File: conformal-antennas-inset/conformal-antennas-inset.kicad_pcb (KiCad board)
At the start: 2 copper layers, 172.5 x 134.5 mm, 1 part, among them J1 Conn_Coaxial

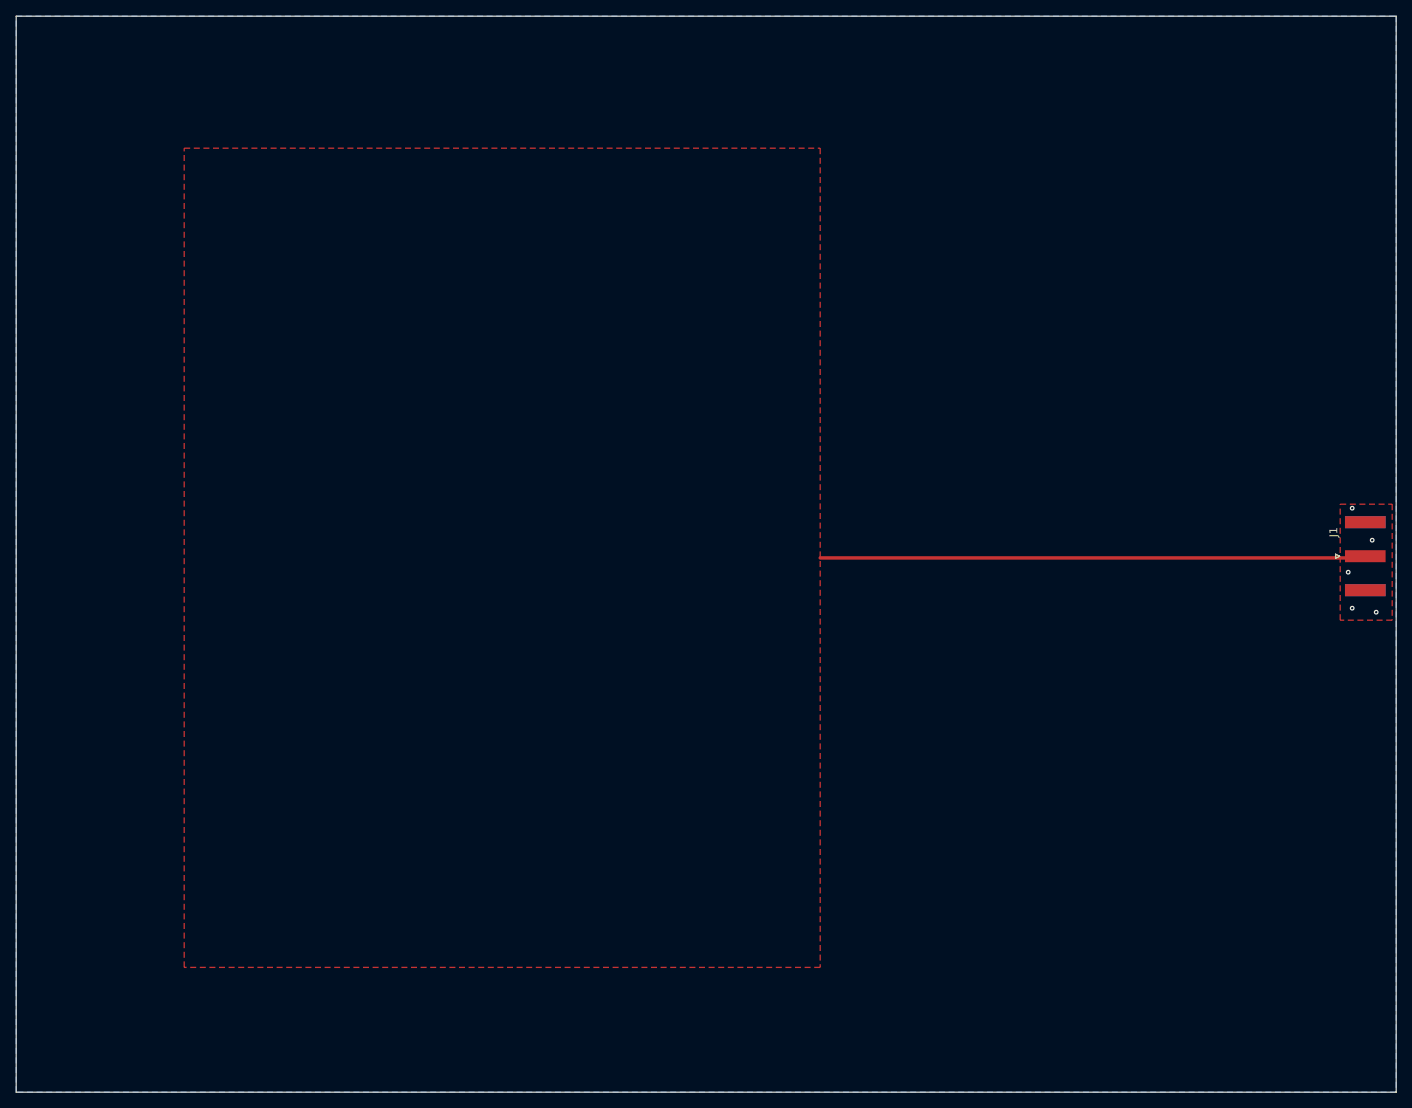
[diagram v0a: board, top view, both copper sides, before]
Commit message: resized ground plane
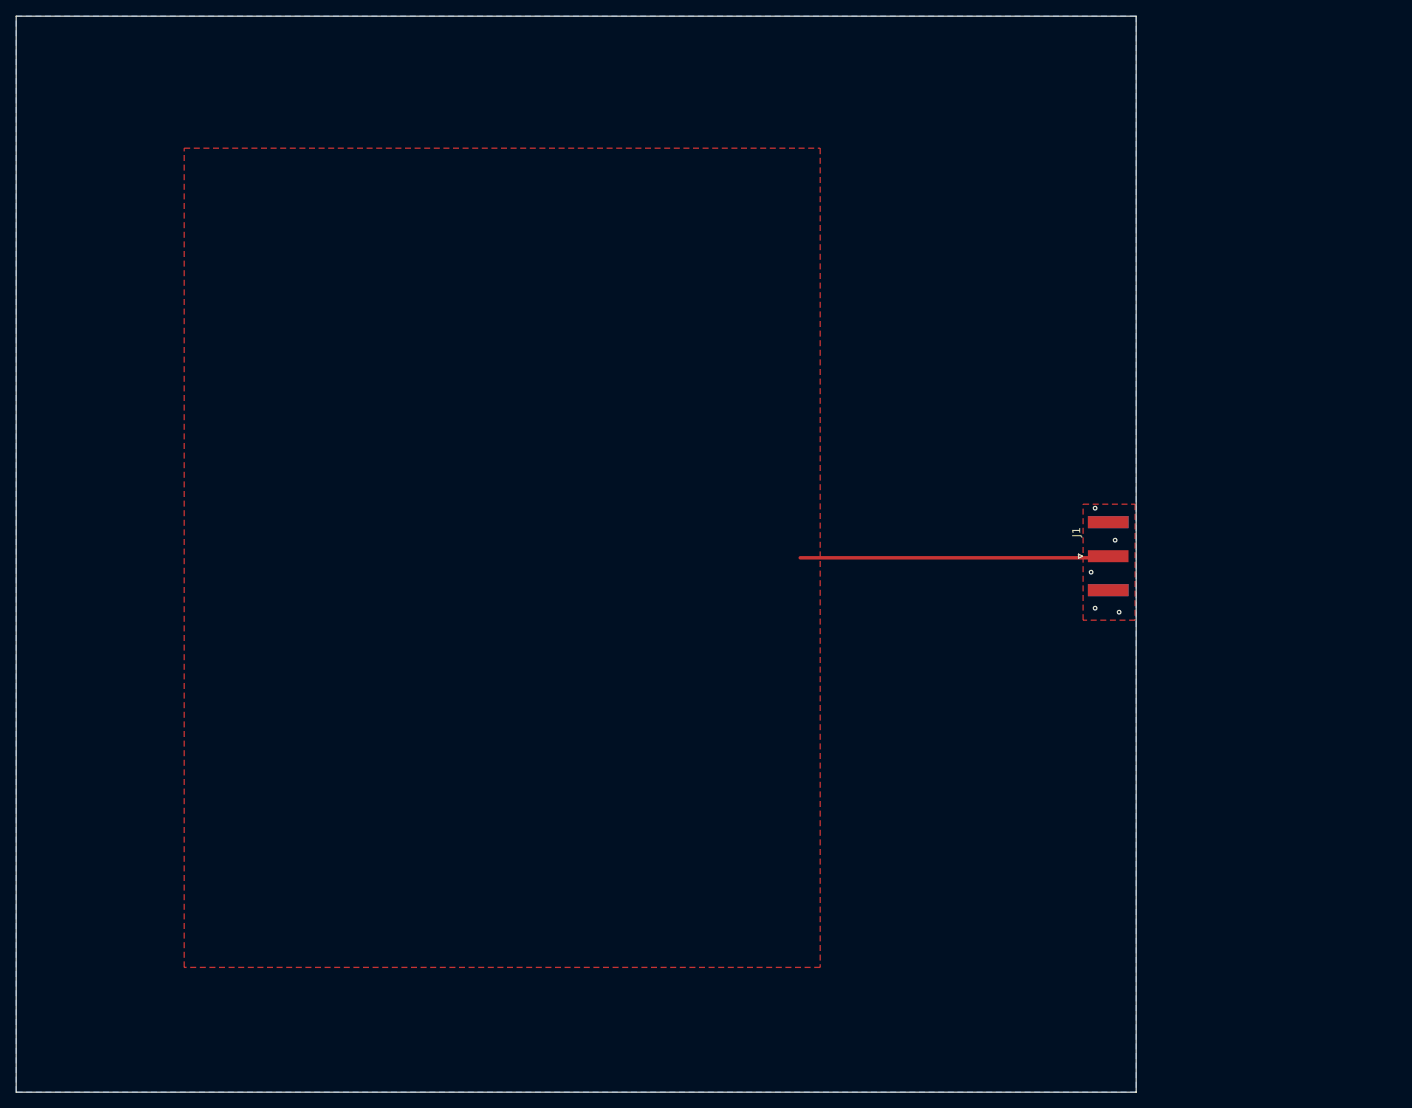
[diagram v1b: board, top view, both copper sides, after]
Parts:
- moved J1 32.1 mm to (185.0, 103.5)
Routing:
- net /Signal: track 68.1 -> 38.5 mm
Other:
- board size 172.5 x 134.5 mm -> 140 x 134.5 mm
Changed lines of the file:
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@@
 	(footprint "Connector_Coaxial:SMA_Amphenol_132289_EdgeMount"
 		(layer "F.Cu")
-		(at 217.1375 103.5)
+		(at 185 103.5)
 		(descr "https://www.amphenolrf.com/library/download/link/link_id/595984/parent/132289/")
 		(tags "SMA")
@@
 	(gr_line
 		(start 48.5 36)
-		(end 221 36)
+		(end 188.5 36)
 		(stroke
 			(width 0.05)
-			(type default)
+			(type solid)
 		)
 		(layer "Edge.Cuts")
 	)
 	(gr_line
-		(start 221 170.5)
+		(start 188.5 170.5)
 		(end 48.5 170.5)
 		(stroke
@@
 	)
 	(gr_line
-		(start 221 36)
-		(end 221 170.5)
+		(start 188.5 36)
+		(end 188.5 170.5)
 		(stroke
 			(width 0.05)
@@
 	)
 	(via
-		(at 215.5 110)
+		(at 183.3625 110)
 		(size 0.6)
 		(drill 0.3)
@@
 	)
 	(via
-		(at 218.5 110.5)
+		(at 186.3625 110.5)
 		(size 0.6)
 		(drill 0.3)
@@
 	)
 	(via
-		(at 218 101.5)
+		(at 185.8625 101.5)
 		(size 0.6)
 		(drill 0.3)
@@
 	)
 	(via
-		(at 215.5 97.5)
+		(at 183.3625 97.5)
 		(size 0.6)
 		(drill 0.3)
@@
 	)
 	(via
-		(at 215 105.5)
+		(at 182.8625 105.5)
 		(size 0.6)
 		(drill 0.3)
@@
 	)
 	(segment
-		(start 217.1375 103.716621)
-		(end 149 103.716621)
+		(start 185 103.5)
+		(end 184.915621 103.584379)
+		(width 0.2)
+		(layer "F.Cu")
+		(net 2)
+	)
+	(segment
+		(start 184.915621 103.700379)
+		(end 146.5 103.700379)
 		(width 0.433242)
 		(layer "F.Cu")
@@
 		(polygon
 			(pts
-				(xy 214 97) (xy 220.5 97) (xy 220.5 111.5) (xy 214 111.5)
+				(xy 181.8625 97) (xy 188.3625 97) (xy 188.3625 111.5) (xy 181.8625 111.5)
 			)
 		)
@@
 		(polygon
 			(pts
-				(xy 48.5 36) (xy 221 36) (xy 221 170.5) (xy 48.5 170.5)
-			)
-		)
+				(xy 48.5 36) (xy 188.5 36) (xy 188.5 170.5) (xy 48.5 170.5)
+			)
+		)
